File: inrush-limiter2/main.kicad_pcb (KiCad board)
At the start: 2 copper layers, 31 parts, among them K1 RELAY_2RT, P1 CONN_01X04, Q1 2N3904, Q2 PN2222A, T1 TRANSFO, U1 LM393, U2 50 ohm NTC

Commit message: update
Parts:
- moved R9 19.2 mm to (144.8, 74.9), turned to 270 degrees
- moved R10 19.0 mm to (149.9, 74.9), turned to 270 degrees
- moved Q1 13.3 mm to (139.7, 90.2), turned to 0 degrees
- moved D6 11.4 mm to (149.9, 90.2), turned to 90 degrees
- moved U1 3.81 mm to (129.5, 83.8)
- moved R3 2.84 mm to (124.5, 83.8)
- moved R2 1.27 mm to (125.7, 72.4)
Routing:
- net +5V: track 60.4 -> 81.0 mm
- net Net-(CP1-Pad1): track 20.9 -> 5.61 mm
- net Net-(D6-Pad1): track 26.0 -> 13.2 mm
- net Net-(Q1-Pad2): track 23.0 -> 33.1 mm
- net Net-(R2-Pad2): track 4.02 -> 0.00 mm
- net GND: track 175.8 -> 177.6 mm

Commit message: update
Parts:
- moved R10 2.84 mm to (147.3, 76.2)
- moved R9 2.84 mm to (142.2, 76.2)
- moved CP1 1.27 mm to (120.7, 76.2)
- moved R3 1.27 mm to (125.7, 83.8)
- moved RVAR1 1.27 mm to (116.8, 73.7)
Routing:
- net GND: track 177.6 -> 231.2 mm
- net Net-(CP1-Pad1): track 5.61 -> 24.7 mm
- net Net-(R2-Pad2): track 0.00 -> 8.67 mm
- net +5V: track 81.0 -> 77.5 mm
- net Net-(Q1-Pad2): track 33.1 -> 30.8 mm
- net Net-(R4-Pad2): track 19.0 -> 17.6 mm
- net Net-(D6-Pad2): track 5.08 -> 4.58 mm

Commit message: update
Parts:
- moved D7 9.67 mm to (138.4, 54.6)
- moved D6 1.27 mm to (149.9, 91.4)
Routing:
- net GND: track 231.2 -> 242.2 mm
- net Net-(D7-Pad1): track 10.5 -> 19.1 mm
- net +5V: track 77.5 -> 84.2 mm
- net Net-(D6-Pad2): track 4.58 -> 5.68 mm
- net Net-(Q2-Pad1): track 5.39 -> 4.34 mm

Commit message: update
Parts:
- moved R7 12.8 mm to (175.3, 61.0), turned to 180 degrees
- moved F1 6.35 mm to (179.1, 77.5)
- moved R8 1.80 mm to (189.2, 62.2)
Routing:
- net AC-neut-low: track 26.9 -> 0.00 mm
- net AC-live-f: track 37.9 -> 29.9 mm
- net Net-(F1-Pad2): track 19.1 -> 16.7 mm
- net +5V: track 84.2 -> 82.4 mm
- net AC-neut: track 31.3 -> 29.5 mm
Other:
- net class Default: trace_width 0.75 -> 1

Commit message: update
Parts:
- moved R8 13.0 mm to (176.5, 59.7)
- moved R7 12.8 mm to (162.6, 59.7), turned to 0 degrees
- moved F1 3.81 mm to (179.1, 81.3)
- moved R3 1.27 mm to (125.7, 85.1)
- moved R2 1.27 mm to (125.7, 73.7)
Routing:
- net AC-neut: track 29.5 -> 38.9 mm
- net AC-live-f: track 29.9 -> 34.0 mm
- net +5V: track 82.4 -> 81.1 mm
- net AC-live-out: track 32.1 -> 33.1 mm
- net Net-(CP1-Pad1): track 24.7 -> 25.5 mm
- net Net-(R2-Pad2): track 8.67 -> 8.15 mm

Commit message: update
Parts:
- removed RVAR1: 1M, Resistors_ThroughHole:Resistor_Horizontal_RM7mm
- added RV1: POT, Potentiometers:Potentiometer_Bourns_3296W_3-8Zoll_Inline_ScrewUp, F.Cu at (116.8, 80.0)
- P1: footprint Connect:AK300-4 -> Terminal_Blocks:TerminalBlock_WAGO-804_RM7.5mm_3pol
- T1: footprint Transformers_CHK:Trafo_CHK-EI30-2VA_1xSec -> Transformers_CHK:Trafo_CHK-EI30-2VA_Neutral
- moved Q2 1.27 mm to (128.3, 54.6)
- moved R1 1.27 mm to (116.8, 59.7)
- moved R11 1.27 mm to (134.6, 59.7)
- moved R12 1.27 mm to (116.8, 55.9)
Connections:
- F1 pad 2: Net-(F1-Pad2) -> (no net)
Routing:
- net AC-live-out: track 33.1 -> 51.7 mm
- net AC-neut: track 38.9 -> 20.9 mm
- net Net-(F1-Pad2): track 16.8 -> 0.00 mm
- net +5V: track 81.1 -> 84.7 mm
- net Net-(CP1-Pad1): track 25.5 -> 23.7 mm
- net Net-(D7-Pad1): track 19.1 -> 17.9 mm
- net Net-(Q2-Pad1): track 4.34 -> 5.08 mm
- net Net-(C1-Pad1): track 22.4 -> 21.9 mm

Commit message: add custom footprint for terminal block
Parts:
- added P2: CONN_01X02, Wire_Pads:SolderWirePad_2x_1-2mmDrill, F.Cu at (156.2, 44.5)
- P1: footprint Terminal_Blocks:TerminalBlock_WAGO-804_RM7.5mm_3pol -> test:fuck
- moved MOV1 15.7 mm to (182.9, 64.8)
- moved P1 12.8 mm to (195.6, 62.2)
- moved R8 2.54 mm to (174.0, 59.7)
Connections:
- F1 pad 2: (no net) -> Net-(F1-Pad2)
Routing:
- net Net-(D2-Pad2): track 3.81 -> 25.9 mm
- net AC-live-out: track 51.7 -> 69.8 mm
- net Net-(F1-Pad2): track 0.00 -> 15.0 mm
- net AC-live-f: track 34.0 -> 30.8 mm
- net AC-neut: track 20.9 -> 22.1 mm

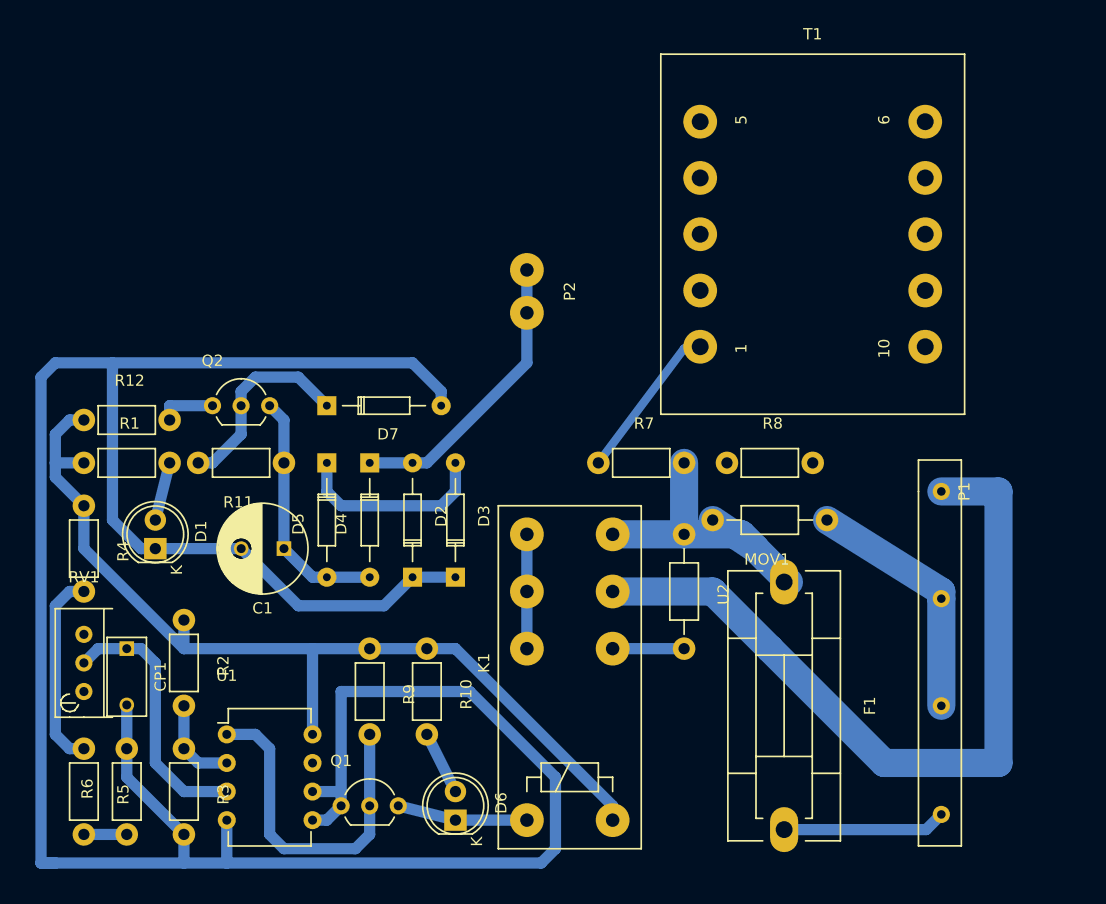
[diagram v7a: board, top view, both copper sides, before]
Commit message: update terminal block outline
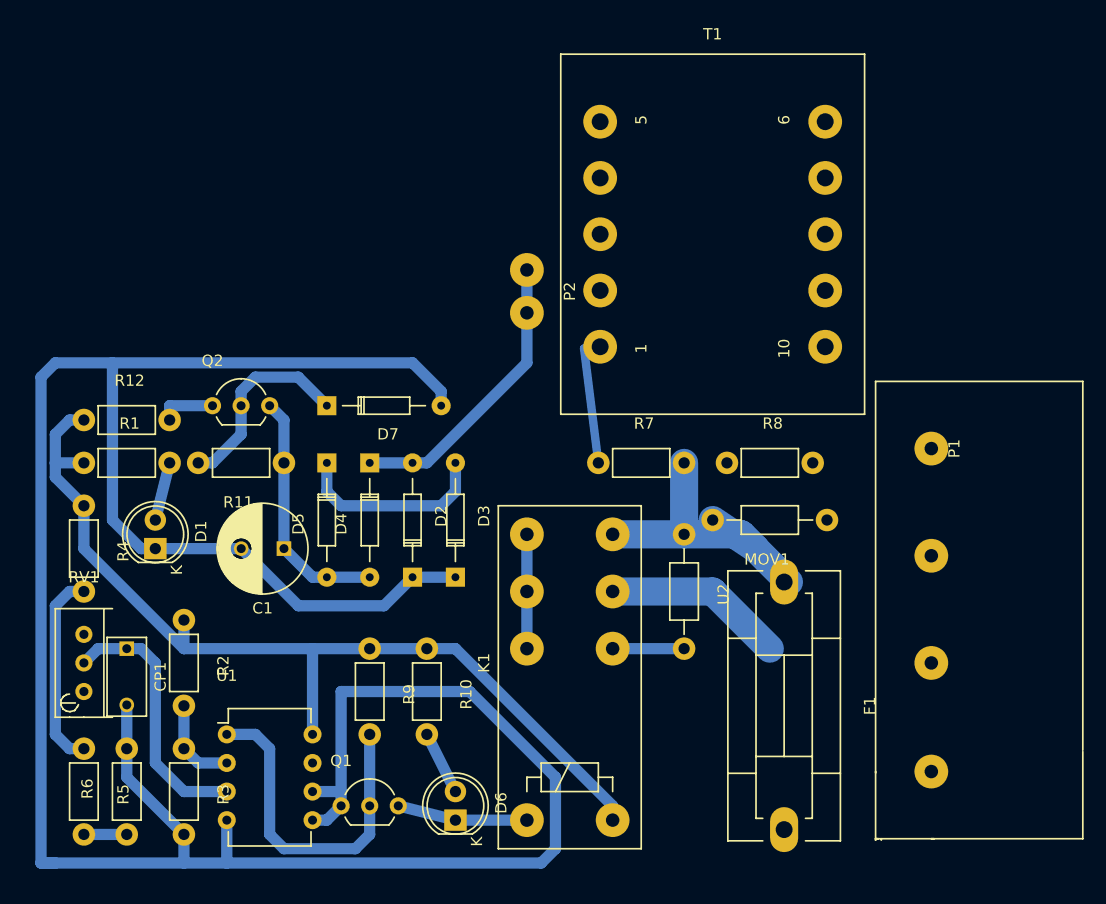
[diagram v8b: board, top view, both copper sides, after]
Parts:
- moved T1 8.89 mm to (172.7, 39.4)
- moved P1 2.84 mm to (198.1, 61.0)
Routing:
- net AC-live-out: track 69.8 -> 16.1 mm
- net AC-neut: track 22.1 -> 0.00 mm
- net Net-(F1-Pad2): track 15.0 -> 0.43 mm
- net AC-live-f-low: track 14.1 -> 11.7 mm
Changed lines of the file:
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@@
   (general
     (links 58)
-    (no_connects 5)
-    (area 110.105 18.665 201.370002 96.28099)
+    (no_connects 9)
+    (area 110.105 -0.678001 203.950002 96.28099)
     (thickness 1.6)
     (drawings 0)
-    (tracks 152)
+    (tracks 143)
     (zones 0)
     (modules 32)
@@
   )
   (module Transformers_CHK:Trafo_CHK-EI30-2VA_Neutral (layer F.Cu)
-    (at 181.61 39.37)
+    (at 172.72 39.37)
     (descr "Trafo, Printtrafo, CHK, EI30, 2VA, neutral,")
     (tags "Trafo, Printtrafo, CHK, EI30, 2VA, neutral,")
@@
     )
   )
-  (module test:fuck (layer F.Cu)
-    (at 195.58 62.23 270)
-    (fp_text reference P1 (at 0 0.5 270) (layer F.SilkS)
-      (effects (font (size 1 1) (thickness 0.15)))
-    )
-    (fp_text value CONN_01X04 (at 0 -0.5 270) (layer F.Fab)
-      (effects (font (size 1 1) (thickness 0.15)))
-    )
-    (fp_line (start 0 4.572) (end 31.496 4.572) (layer F.SilkS) (width 0.15))
-    (fp_line (start 31.496 4.572) (end 31.496 0.762) (layer F.SilkS) (width 0.15))
-    (fp_line (start 31.496 0.762) (end -2.794 0.762) (layer F.SilkS) (width 0.15))
-    (fp_line (start -2.794 0.762) (end -2.794 4.572) (layer F.SilkS) (width 0.15))
-    (fp_line (start -2.794 4.572) (end 0 4.572) (layer F.SilkS) (width 0.15))
-    (pad 1 thru_hole circle (at 0 2.54 270) (size 1.524 1.524) (drill 0.762) (layers *.Cu *.Mask F.SilkS)
-      (net 5 AC-live-out))
-    (pad 2 thru_hole circle (at 9.525 2.54 270) (size 1.524 1.524) (drill 0.762) (layers *.Cu *.Mask F.SilkS)
-      (net 6 AC-neut))
-    (pad 3 thru_hole circle (at 19.05 2.54 270) (size 1.524 1.524) (drill 0.762) (layers *.Cu *.Mask F.SilkS)
-      (net 6 AC-neut))
-    (pad 4 thru_hole circle (at 28.702 2.54 270) (size 1.524 1.524) (drill 0.762) (layers *.Cu *.Mask F.SilkS)
-      (net 23 "Net-(F1-Pad2)"))
-  )
   (module Wire_Pads:SolderWirePad_2x_1-2mmDrill (layer F.Cu)
     (at 156.21 44.45 270)
@@
     (pad 1 thru_hole circle (at 1.905 0 270) (size 2.99974 2.99974) (drill 1.19888) (layers *.Cu *.Mask F.SilkS)
       (net 4 "Net-(D2-Pad2)"))
+  )
+  (module test:fuck (layer F.Cu)
+    (at 198.12 60.96 270)
+    (fp_text reference P1 (at -2.54 3.929 270) (layer F.SilkS)
+      (effects (font (size 1 1) (thickness 0.15)))
+    )
+    (fp_text value CONN_01X04 (at -2.54 2.929 270) (layer F.Fab)
+      (effects (font (size 1 1) (thickness 0.15)))
+    )
+    (fp_line (start -8.509 -7.493) (end -8.509 10.922) (layer F.SilkS) (width 0.15))
+    (fp_line (start 26.289 10.922) (end -8.509 10.922) (layer F.SilkS) (width 0.15))
+    (fp_line (start 24.384 -7.493) (end 32.131 -7.493) (layer F.SilkS) (width 0.15))
+    (fp_line (start 24.257 -7.493) (end -8.509 -7.493) (layer F.SilkS) (width 0.15))
+    (fp_line (start 32.258 10.922) (end 32.131 10.922) (layer F.SilkS) (width 0.15))
+    (fp_line (start 32.131 10.922) (end 32.131 -7.493) (layer F.SilkS) (width 0.15))
+    (fp_line (start 32.131 10.922) (end 32.131 10.668) (layer F.SilkS) (width 0.15))
+    (fp_line (start 26.162 10.922) (end 32.258 10.922) (layer F.SilkS) (width 0.15))
+    (fp_line (start 32.258 10.414) (end 32.131 10.414) (layer F.SilkS) (width 0.15))
+    (fp_line (start 32.131 5.969) (end 32.131 5.715) (layer F.SilkS) (width 0.15))
+    (pad 1 thru_hole circle (at -2.54 5.969 270) (size 3 3) (drill 1.2) (layers *.Cu *.Mask F.SilkS)
+      (net 5 AC-live-out))
+    (pad 2 thru_hole circle (at 6.985 5.969 270) (size 3 3) (drill 1.2) (layers *.Cu *.Mask F.SilkS)
+      (net 6 AC-neut))
+    (pad 3 thru_hole circle (at 16.51 5.969 270) (size 3 3) (drill 1.2) (layers *.Cu *.Mask F.SilkS)
+      (net 6 AC-neut))
+    (pad 4 thru_hole circle (at 26.162 5.969 270) (size 3 3) (drill 1.2) (layers *.Cu *.Mask F.SilkS)
+      (net 23 "Net-(F1-Pad2)"))
   )
   (segment (start 133.35 54.61) (end 134.62 55.88) (width 1) (layer B.Cu) (net 1) (status 10))
@@
   (segment (start 142.24254 59.69052) (end 146.04642 59.69052) (width 1) (layer B.Cu) (net 4) (status 30))
   (segment (start 146.04642 59.69052) (end 146.04746 59.68948) (width 1) (layer B.Cu) (net 4) (status 30))
-  (segment (start 193.04 62.23) (end 198.12 62.23) (width 2.5) (layer B.Cu) (net 5))
-  (segment (start 187.96 86.36) (end 177.8 76.2) (width 2.5) (layer B.Cu) (net 5))
-  (segment (start 198.12 86.36) (end 187.96 86.36) (width 2.5) (layer B.Cu) (net 5))
-  (segment (start 198.12 62.23) (end 198.12 86.36) (width 2.5) (layer B.Cu) (net 5))
   (segment (start 172.72 71.12) (end 177.8 76.2) (width 2.5) (layer B.Cu) (net 5))
   (segment (start 163.83 71.12) (end 172.72 71.12) (width 2.5) (layer B.Cu) (net 5) (status 10))
-  (segment (start 193.04 71.755) (end 193.04 71.12) (width 2.5) (layer B.Cu) (net 6))
-  (segment (start 193.04 71.12) (end 182.88 64.77) (width 2.5) (layer B.Cu) (net 6) (status 20))
-  (segment (start 193.04 81.28) (end 193.04 71.755) (width 2.5) (layer B.Cu) (net 6))
   (segment (start 142.24 83.82) (end 142.24 90.17) (width 1) (layer B.Cu) (net 7) (status 30))
   (segment (start 134.62 93.98) (end 140.97 93.98) (width 1) (layer B.Cu) (net 7))
@@
   (segment (start 115.57 71.12) (end 114.3 72.39) (width 1) (layer B.Cu) (net 8))
   (segment (start 170.18 76.2) (end 163.83 76.2) (width 1) (layer B.Cu) (net 9) (status 30))
-  (segment (start 162.56 59.69) (end 170.18 49.53) (width 0.75) (layer B.Cu) (net 11) (status 30))
-  (segment (start 170.18 49.53) (end 171.61002 49.36998) (width 0.75) (layer B.Cu) (net 11) (status 30))
+  (segment (start 162.56 59.69) (end 161.29 49.53) (width 0.75) (layer B.Cu) (net 11) (status 20))
+  (segment (start 161.29 49.53) (end 162.72002 49.36998) (width 0.75) (layer B.Cu) (net 11) (status 30))
   (segment (start 147.32 83.82) (end 149.86 88.9) (width 1) (layer B.Cu) (net 12) (status 20))
   (segment (start 130.81 54.61) (end 130.81 57.15) (width 1) (layer B.Cu) (net 13) (status 10))
@@
   (segment (start 142.24 76.2) (end 137.16 76.2) (width 1) (layer B.Cu) (net 22) (status 10))
   (segment (start 147.32 76.2) (end 142.24 76.2) (width 1) (layer B.Cu) (net 22) (status 30))
-  (segment (start 179.07 92.28074) (end 191.69126 92.28074) (width 1) (layer B.Cu) (net 23))
-  (segment (start 191.69126 92.28074) (end 193.04 90.932) (width 1) (layer B.Cu) (net 23))
   (segment (start 179.49926 92.28074) (end 179.07 92.28074) (width 1) (layer B.Cu) (net 23) (status 30))
 )
